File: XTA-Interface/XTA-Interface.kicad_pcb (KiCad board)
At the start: 2 copper layers, 99.9 x 99.9 mm, 19 parts, among them CN1 DRIVE 0, CN2 DRIVE 1, CN3 LEDs, CN4 Drive Power, J3 Bus_ISA_8bit, U1 BIOS FLASH, U2 74HCT245, U3 ATF/GAL16V8-15 "LEFT", U4 ATF/GAL16V8-15 "RIGHT"

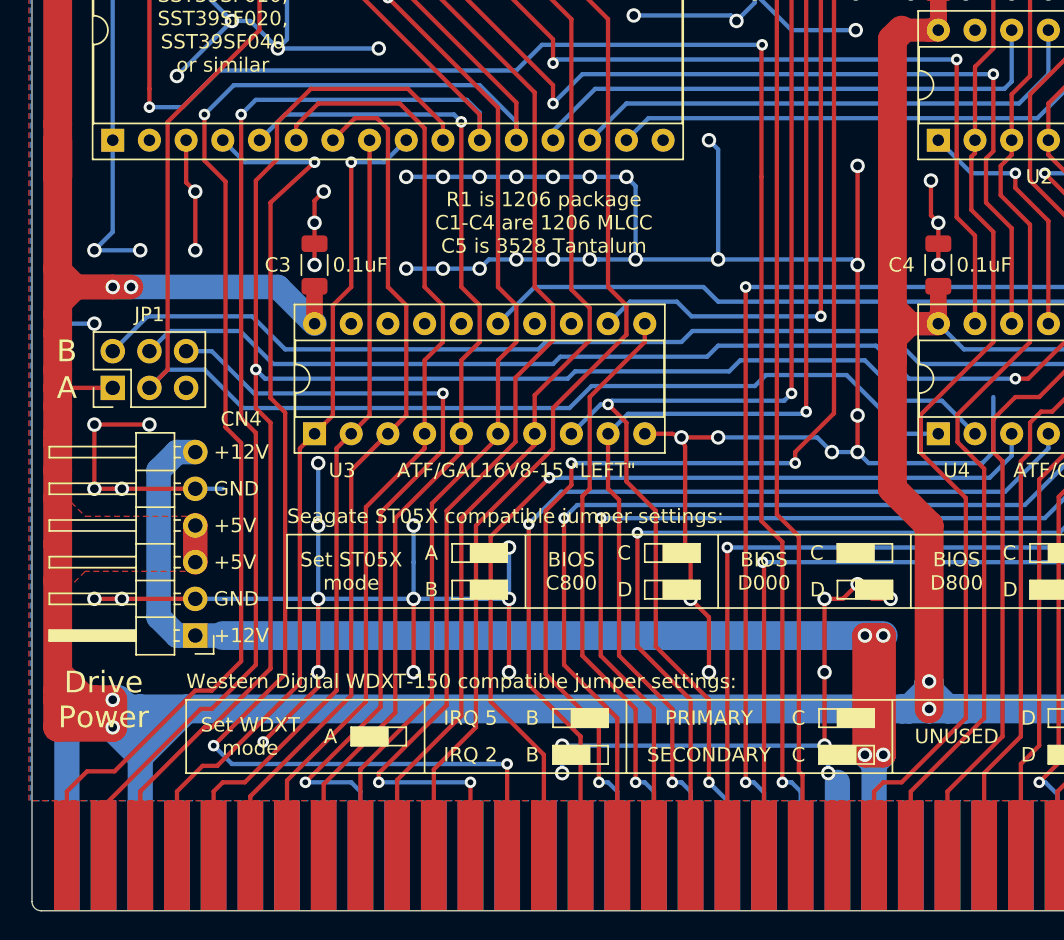
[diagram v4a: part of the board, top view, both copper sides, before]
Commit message: Swap positions of A and B jumpers.
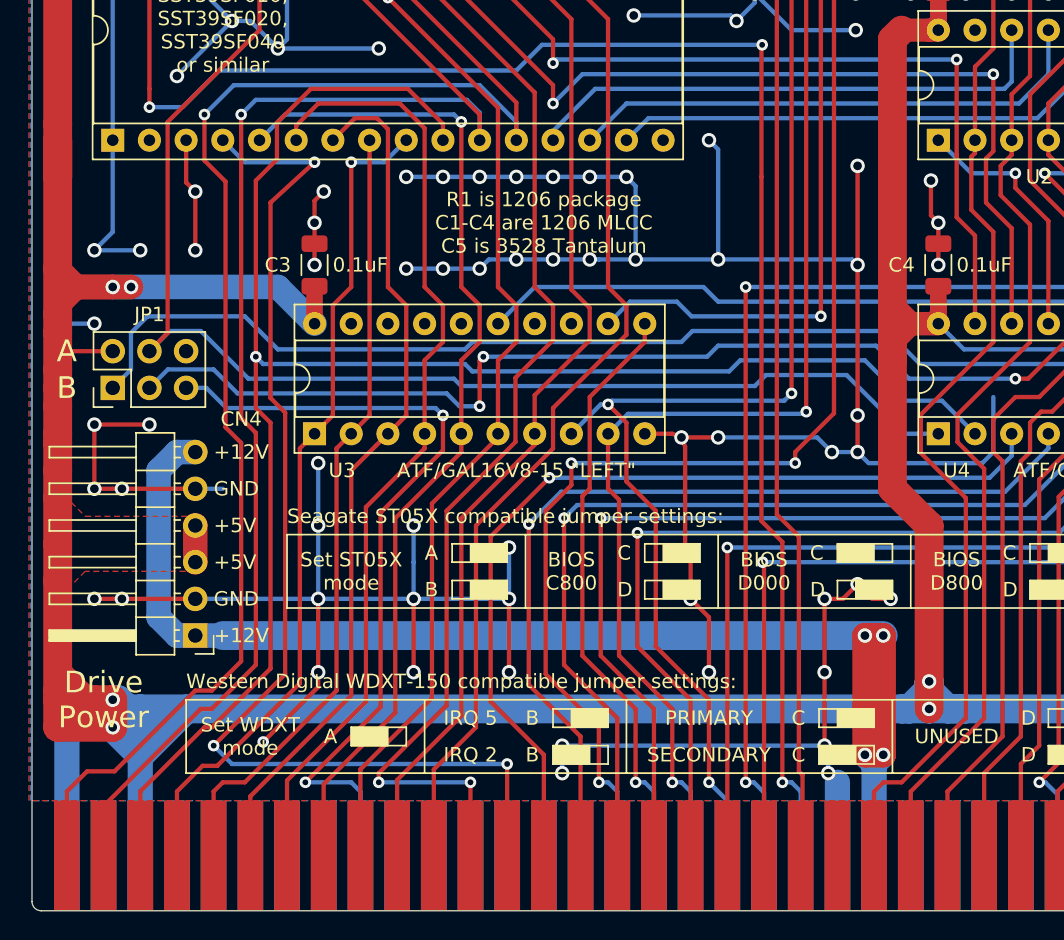
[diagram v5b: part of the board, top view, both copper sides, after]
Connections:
- JP1 pad 1: VCC -> IRQ2
- JP1 pad 2: IRQ2 -> VCC
- JP1 pad 3: ST_WD_JUMPER -> XTA_IRQ
- JP1 pad 4: XTA_IRQ -> ST_WD_JUMPER
- JP1 pad 5: GND -> IRQ5
- JP1 pad 6: IRQ5 -> GND
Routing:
- net XTA_IRQ: track 126.6 -> 129.7 mm, vias 1 -> 3
- net ST_WD_JUMPER: track 94.4 -> 91.8 mm
- net IRQ2: track 115.8 -> 118.4 mm
- net IRQ5: track 58.4 -> 56.4 mm

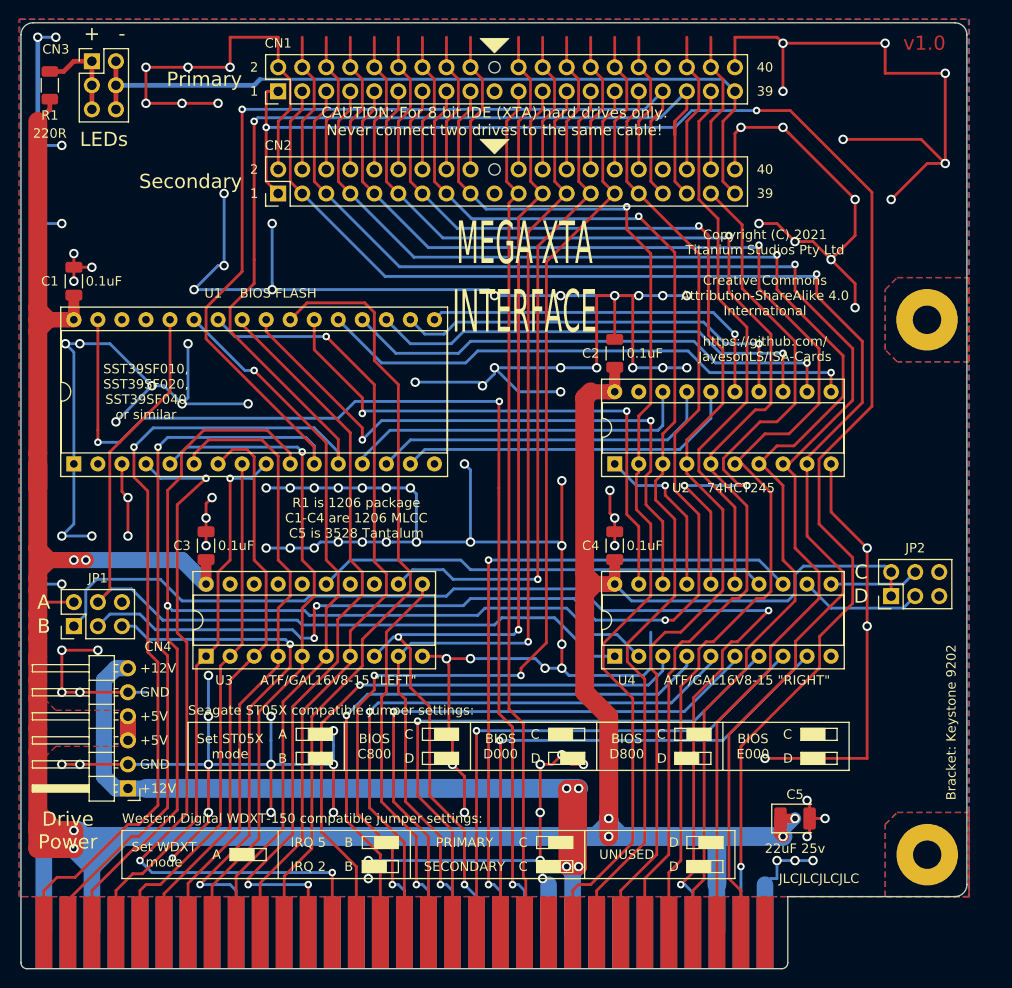
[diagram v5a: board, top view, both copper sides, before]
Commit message: XTA-Interface: Fix rear bracket hole locations. Board is now 102mm wide. Also route address line changes previosly made to schematic.
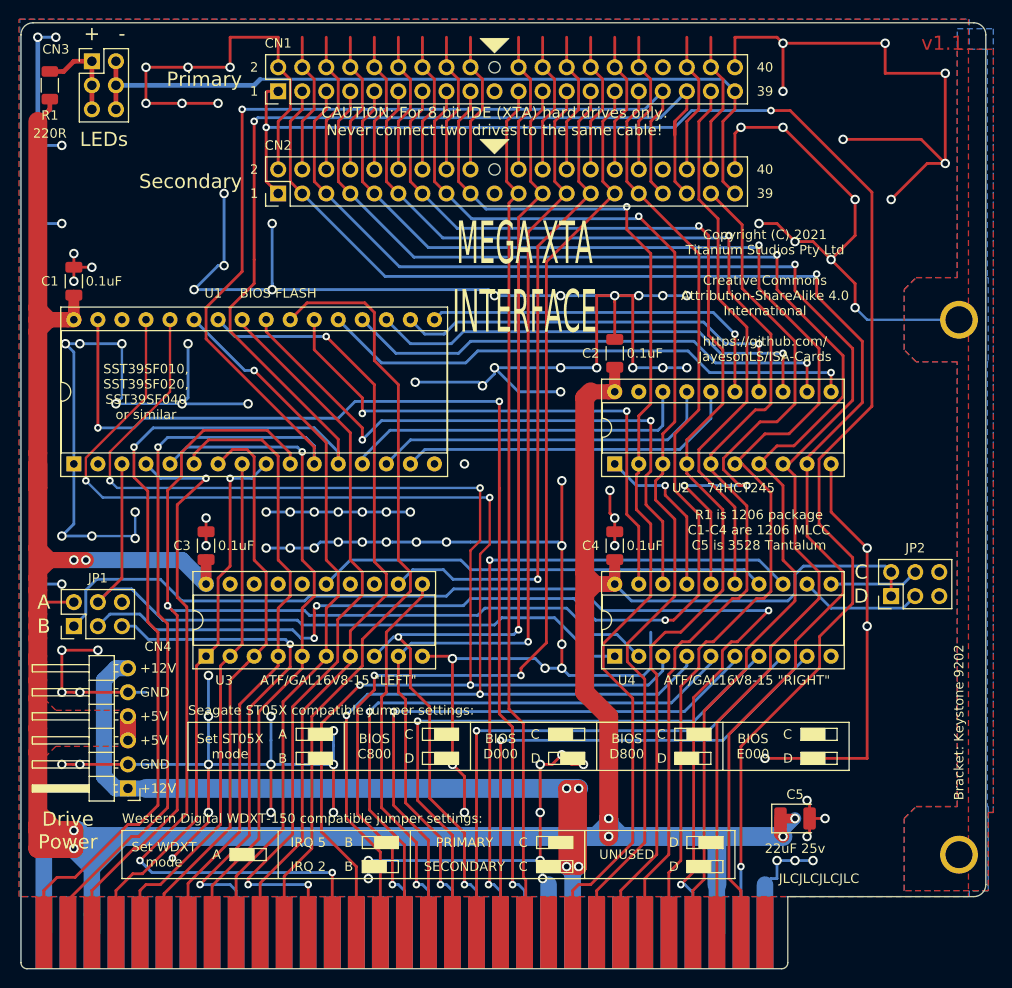
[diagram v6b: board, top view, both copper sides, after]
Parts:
- moved H2 3.38 mm to (195.8, 73.7)
- moved H4 3.36 mm to (195.8, 130.2)
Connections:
- U1 pad 28: ST_WD_JUMPER -> A13
- U1 pad 29: GND -> A14
- U1 pad 3: GND -> ST_WD_JUMPER
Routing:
- net A14: track 63.6 -> 147.9 mm, vias 1 -> 4
- net A13: track 63.5 -> 143.9 mm, vias 1 -> 4
- net ST_WD_JUMPER: track 91.8 -> 74.4 mm
- net GND: track 1024.2 -> 1017.5 mm, vias 125 -> 123
- net ~MEMW: track 114.8 -> 113.1 mm
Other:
- board size 99.9 x 99.9 mm -> 101.9 x 99.9 mm
- board text added: "v1.1"
- board text removed: "v1.0"

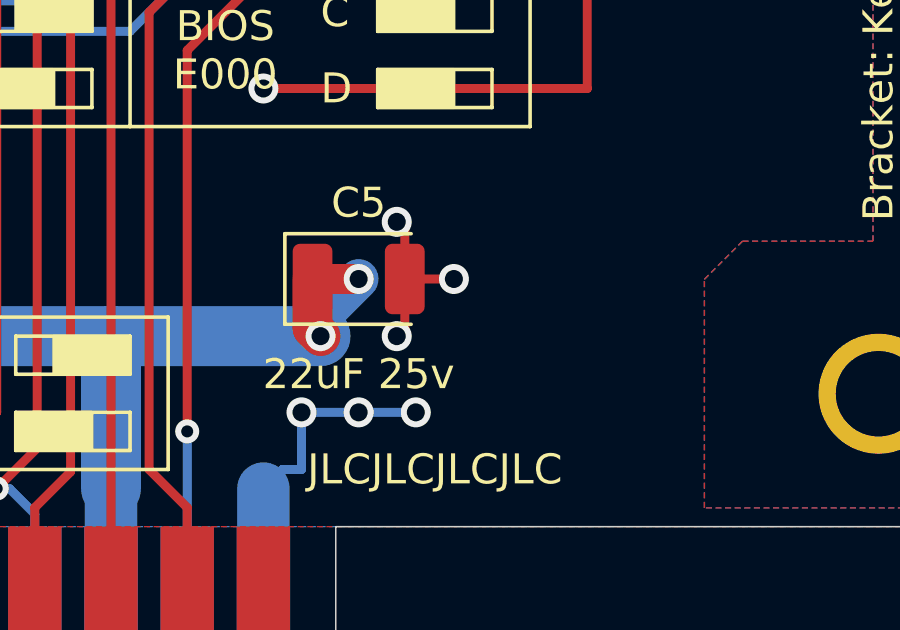
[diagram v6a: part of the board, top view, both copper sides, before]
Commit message: XTA-Interface: Change tantalum capacitor value text.
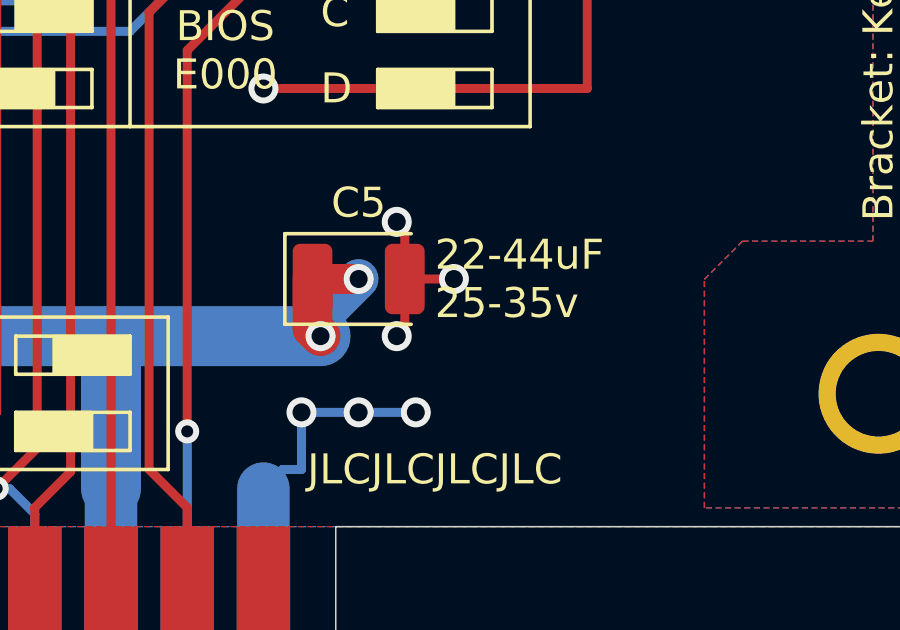
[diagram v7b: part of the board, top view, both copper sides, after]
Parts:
- C5: value 22uF 25v -> 22-44uF, 25-35v
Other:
- board text added: "22-44uF 25-35v"

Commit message: Update boards.
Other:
- board text added: "Created by Jayeson Lee-Steere https://github.com/ JayesonLS/ISA-Cards"
- board text removed: "Copyright (C) 2021 Titanium Studios Pty Ltd Creative Commons Attribution-ShareAlike 4.0 International https://github.com/ JayesonLS/ISA-Cards"
